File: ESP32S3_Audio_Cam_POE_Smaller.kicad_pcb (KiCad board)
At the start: 4 copper layers, 83.2 x 32.4 mm, 50 parts, among them CN1 PJ-316C-6A, J1 Conn_01x20_Pin, J10 Conn_01x02, J2 Conn_01x20_Pin, U11 TM1637, U15 MAX98357AETE+T, U16 ICS-43434, U17 ICS-43434

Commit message: Draft smaller board.
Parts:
- added JP1: SolderJumper_3_Bridged12, Jumper:SolderJumper-3_P1.3mm_Bridged12_Pad1.0x1.5mm, F.Cu at (89.5, 159.4)
- added TP1: TestPoint, Connector_PinHeader_1.00mm:PinHeader_1x01_P1.00mm_Vertical, F.Cu at (92.7, 155.6)
- JP3, JP4, JP5, JP6: moved to F.Cu
- TP47, TP49, TP56, TP57, TP63, TP64, TP85: footprint Project-specific:TestPoint_Pad_D1.0mm -> TestPoint:TestPoint_Pad_D1.0mm
- TP66, TP67: footprint Project-specific:TestPoint_Pad_D1.0mm -> TestPoint:TestPoint_Pad_D1.0mm; moved to B.Cu
- moved TP47 117.7 mm to (155.8, 158.6)
- moved C45 114.3 mm to (144.1, 147.3), turned to 0 degrees
- moved R39 114.3 mm to (146.7, 147.3), turned to 0 degrees
- moved TP57 114.2 mm to (155.2, 148.6)
- moved C47 113.8 mm to (145.7, 146.1), turned to 0 degrees
- moved U16 113.8 mm to (88.6, 142.1)
- moved C69 113.8 mm to (84.7, 142.8)
- moved JP7 113.8 mm to (88.6, 145.3)
- moved TST-R20 113.8 mm to (84.7, 144.0)
- moved TST-R26 113.8 mm to (84.7, 141.5)
- moved C44 113.5 mm to (148.1, 146.1), turned to 0 degrees
- moved U11 113.2 mm to (148.0, 154.1)
- moved TP56 111.6 mm to (153.3, 145.7)
- moved R38 111.5 mm to (146.7, 144.8), turned to 0 degrees
- moved TST-R14 110.3 mm to (148.1, 142.2), turned to 0 degrees
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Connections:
- net Net-(C54-Pad1) renamed /V.SPK
- J1 pad 15: /SPK.BCLK -> /SPK.DIN
- J1 pad 16: /SPK.DIN -> /SPK.BCLK
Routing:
- net +3V3: track 0.00 -> 175.2 mm
- net /MIC.WS: track 0.00 -> 95.3 mm, vias 0 -> 2
- net /MIC.SCK: track 0.00 -> 94.6 mm, vias 0 -> 2
- net /MIC.SD: track 0.00 -> 93.4 mm, vias 0 -> 2
- net /7SEG.SEG1: track 0.00 -> 62.0 mm, vias 0 -> 2
- net /7SEG.SEG3: track 0.00 -> 52.9 mm, vias 0 -> 2
- net /7SEG.SEG2: track 0.00 -> 49.3 mm, vias 0 -> 2
- net /7SEG.GRID1: track 0.00 -> 43.4 mm, vias 0 -> 2
- net /SPK.DIN: track 0.00 -> 43.0 mm
- net /7SEG.SEG6: track 0.00 -> 42.5 mm, vias 0 -> 2
- net /7SEG.DIO: track 0.00 -> 42.0 mm
- net /SPK.BCLK: track 0.00 -> 40.3 mm
- net /7SEG.K1: track 0.00 -> 40.0 mm
- net /7SEG.SEG5: track 0.00 -> 39.5 mm, vias 0 -> 2
- net /7SEG.SEG7: track 0.00 -> 38.9 mm, vias 0 -> 2
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- removed copper zone on In2.Cu, net (none)
- removed copper zone on In2.Cu, net +3V3
- removed copper zone on In1.Cu, net COM
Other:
- board size 83.2 x 32.4 mm -> 97.5 x 45.7 mm
- copper layers 4 -> 2

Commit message: Added smaller production files.
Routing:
- net /MIC.SD: track 93.4 -> 94.6 mm
- net COM: vias 41 -> 99

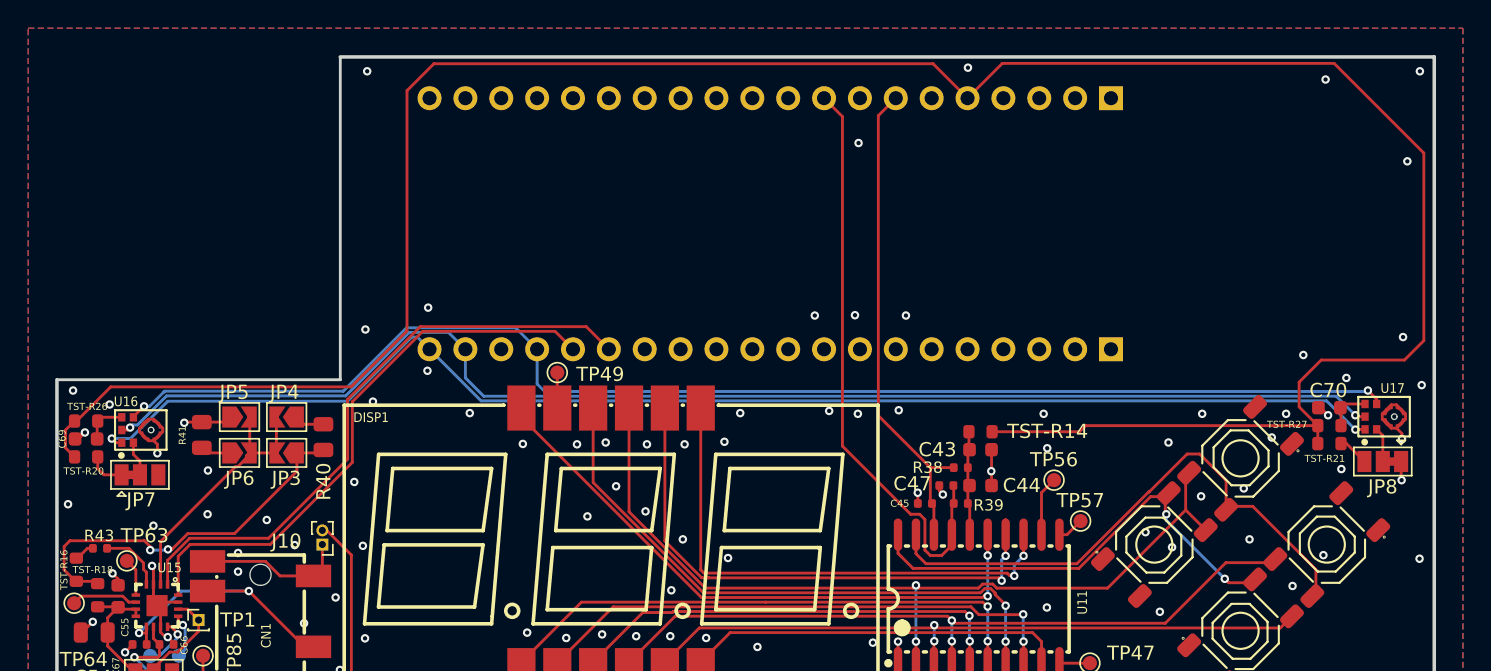
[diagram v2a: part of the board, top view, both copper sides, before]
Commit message: updated smaller board layout
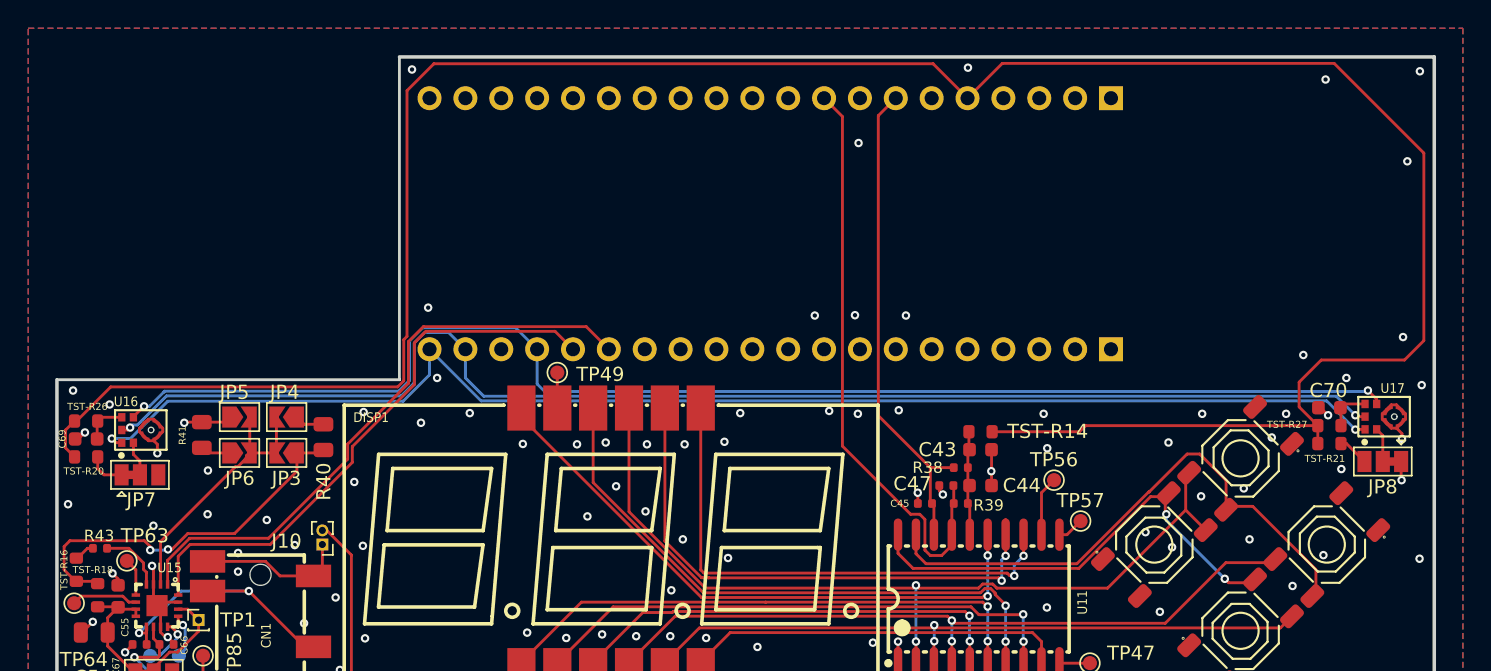
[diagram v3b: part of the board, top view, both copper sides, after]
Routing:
- net +3V3: track 175.2 -> 177.1 mm
- net /MIC.SD: track 94.6 -> 96.2 mm
- net /MIC.SCK: track 94.6 -> 96.3 mm
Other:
- outline, holes or cut-outs redrawn
